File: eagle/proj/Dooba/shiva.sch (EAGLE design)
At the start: 55 parts, among them J1 DM3D-SFDM, J2 USB-BAMPHENOL-MICRO, U1 STM32F030X-LQFP48LQFP48, U2 TPS61200S-PVSON-N10, U3 MAX1811SO8, U4 FT232RQFN32, U5 SN74LVC1G125SOT23-5, U6 SN74LVC1G125SOT23-5, U7 LP3985SOT23-5, U8 LP3985SOT23-5, X1 8MHz

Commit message: Added some parts to Eagle Library Further designed Shiva MP3 Player schematic
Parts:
- added C30, C31: 27pF, dooba:CAP0805
- added C32, C33, C34, C35, C36: 100nF, dooba:CAP0805
- added C37: 470pF, dooba:CAP0805
- added C38: 4.7nF, dooba:CAP0805
- added R11: 1M, dooba:RES0805
- added R12, R13: 4.7R, dooba:RES0805
- added R14: 10k, dooba:RES0805
- added R15: 1k, dooba:RES0805
- added U10: CS4334, dooba:CS4334
- added U11: LM4811PDSO-10, dooba:LM4811PDSO-10
- added U9: STA013LQFP44, dooba:STA013LQFP44
- added X2: 14.7456MHz, dooba:XTAL_GNDSMD_3225
- X1: value 8MHz -> 16MHz; device dooba:XTALSMD-5X32 -> dooba:XTAL_GNDSMD_3225
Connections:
- net N$10 renamed MICROSD_SCK
- net N$11 renamed MICROSD_MISO
- net N$12 renamed MICROSD_DET
- net N$29 renamed STM32F0_TX
- net N$30 renamed STM32F0_RX
- net N$8 renamed !MICROSD_CS
- net N$9 renamed MICROSD_MOSI
- net RX renamed FT232R_RX
- net TX renamed FT232R_TX
- net VIN renamed 5.5V
- removed net CTS: U4.!CTS
- new net 3.3V-CORE: C1.1, C11.1, C12.1, C13.1, C2.1, C26.1, C3.1, C32.2, C33.2, C34.2, C35.2, C4.1, C5.1, C6.2, C7.2, C8.1, R13.1, R14.2, U1.VCC@1, U1.VCC@24, U1.VCC@48, U1.VCCA, U5.!OE, U5.VCC, U7.VOUT, U9.!SRC_INT, U9.!TESTEN, U9.BIT_EN, U9.VDD_1, U9.VDD_2, U9.VDD_3, U9.VDD_4
- new net 3.3V-EXT: C14.2, C15.2, C16.2, C29.1, J1.VCC, R1.1, U8.VOUT
- new net N$11: C37.2, R15.1, U9.FILT
- new net N$2: C31.2, R11.1, U9.XTI, X2.1
- new net N$6: C36.1, R13.2, U9.PVDD
- new net N$8: R14.1, U9.!RESET
- new net N$9: C38.2, R15.2
- net GND: now also C30.1, C31.1, C32.1, C33.1, C34.1, C35.1, C37.1, C38.1, J1.DET_B, J1.GND, R12.2, U9.SCANEN, U9.VSS_1, U9.VSS_2, U9.VSS_3, U9.VSS_4, U9.VSS_5, X1.GND0, X1.GND1, X2.GND0, X2.GND1; no longer R1.1
- net N$3: now also C30.2, R11.2, U9.XTO, X2.2; no longer C14.2, C15.2, C16.2, C29.1, J1.DET_B, J1.VCC, U8.VOUT
- net N$7: now also C36.2, R12.1, U9.PVSS; no longer C1.1, C11.1, C12.1, C13.1, C2.1, C26.1, C3.1, C4.1, C5.1, C6.2, C7.2, C8.1, U1.VCC@1, U1.VCC@24, U1.VCC@48, U1.VCCA, U5.!OE, U5.VCC, U7.VOUT
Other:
- note added: "Boost Circuit Pumps up Battery Voltage to 5.5V"
- note added: "Core Regulator Provides 3.3V to Core Logic blocks: - STM32F030 - STA013"
- note added: "Extra Regulator Provides 3.3V to Extra blocks: - OLED Display - MicroSD Card"
- note added: "MicroSD Adapter Exposes SPI Interface to STM32F0"
- note added: "USB-Serial Level Switcher Bridges FT232R UART (5V) with STM32F0 UART (3.3V)"
- note removed: "Boost Circuit Pumps up Battery Voltage to 5.5V Serves VIN"
- moved on the sheet: BATT(VCC-GND), C10, C14, C15, C16, C21, C25, C26, C27, C28, C29, C9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

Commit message: Added OLED Display to Shiva MP3 Player Started adding button interface
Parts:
- added C39, C40, C41, C47, C48, C49, C50, C51, C52: CAP_POLARIZEDSMD_RADIAL_43, dooba:CAP_POLARIZEDSMD_RADIAL_43
- added C42, C43, C44: CAP0805, dooba:CAP0805
- added C45, C46: 1uF, dooba:CAP0805
- added J3: SJ1-3523N, dooba:SJ1-3523N
- added J4: ADAFRUIT_OLED_13, dooba:ADAFRUIT_OLED_13
- added R16, R17, R18, R19, R22: RES0805, dooba:RES0805
- added R20, R21, R23, R24, R25, R26, R27, R28, R29: 10k, dooba:RES0805
- added SW1: LEFT, dooba:TACTSWCK_PTS_830
- added SW2: UP, dooba:TACTSWCK_PTS_830
- added SW3: CENTER, dooba:TACTSWCK_PTS_830
- added SW4: DOWN, dooba:TACTSWCK_PTS_830
- added SW5: RIGHT, dooba:TACTSWCK_PTS_830
- added SW6: VOL_UP, dooba:TACTSWCK_PTS_830
- added SW7: VOL_DN, dooba:TACTSWCK_PTS_830
- added U12: 5.0V, dooba:LP3985SOT23-5
- U7, U8: value LP3985SOT23-5 -> 3.3V
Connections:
- net 3.3V-EXT renamed 3.3V-MICROSD
- new net !STA013_RST: R14.1, U1.PA3, U9.!RESET
- new net 5.0V-AUDIO: C39.2, C42.1, C46.1, C47.2, R22.2, U10.VA, U11.VCC, U12.VOUT
- new net AMP_SHUTDOWN: R22.1, U1.PA2, U11.SHUTDOWN
- new net AMP_VOL_CLK: U1.PA1, U11.CLOCK
- new net AMP_VOL_UPDN: U1.PA0, U11.UP/DN
- new net AOUT_L: C43.1, C51.1, R17.2
- new net AOUT_R: C44.2, C52.1, R16.2
- new net I2C_SCL: J4.CLK, R20.2, U1.PB6, U9.SCL
- new net I2C_SDA: J4.DATA, R21.2, U1.PB7, U9.SDA
- new net N$10: C40.2, R18.1, U10.AOUTL
- new net N$12: C41.2, R19.2, U10.AOUTR
- new net N$28: C41.1, R16.1
- new net N$29: C40.1, R17.1
- new net N$30: C48.2, U11.VOUT1
- new net N$31: C49.2, U11.VOUT2
- new net N$32: C50.2, U11.BYPASS
- new net N$34: C49.1, J3.RING
- new net N$39: C51.2, U11.VIN1
- new net N$40: C52.2, U11.VIN2
- new net OLED_RST: J4.RST, U1.PA4
- new net STA013_DREQ: U1.PA6, U9.OUT_CLK/DATA_REC
- new net STA013_LRCKT: U10.LRCK, U9.LRCKT
- new net STA013_OCLK: U10.MCLK, U9.OCLK
- new net STA013_SCKR: U1.PA5, U9.SCKR
- new net STA013_SCKT: U10.DEM/SCLK, U9.SCKT
- new net STA013_SDI: U1.PA7, U9.SDI
- new net STA013_SDO: U10.SDATA, U9.SDO
- net 5.5V: now also C45.1, J4.VIN, U12.EN, U12.VIN
- net GND: now also C39.1, C42.2, C43.2, C44.1, C45.2, C46.2, C47.1, C50.1, J3.SLEEVE, J4.GND, R18.2, R19.1, R20.1, R21.1, U10.AGND, U11.GND, U12.GND
- net N$8: now also C48.1, J3.TIP; no longer R14.1, U9.!RESET
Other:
- note added: "128x64 Monochrome OLED Provides UI"
- note added: "Audio Regulator Provides 5.0V to Audio blocks: - D/A Converter - Headphone Amp"
- note added: "CS4334 DAC Converts Digital Audio from STA013 Feeds Analog Audio to Headphone Amplifier"
- note added: "LM4811 Headphone Amplifier Provides Volume Control"
- note added: "MicroSD Regulator Provides 3.3V to the MicroSD Card"
- note added: "STA013 MP3 Decoder Provides Digital Audio Output to DAC"
- note removed: "Extra Regulator Provides 3.3V to Extra blocks: - OLED Display - MicroSD Card"
- moved on the sheet: BATT(VCC-GND), C1, C10, C11, C12, C13, C14, C15, C16, C17, C18, C19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

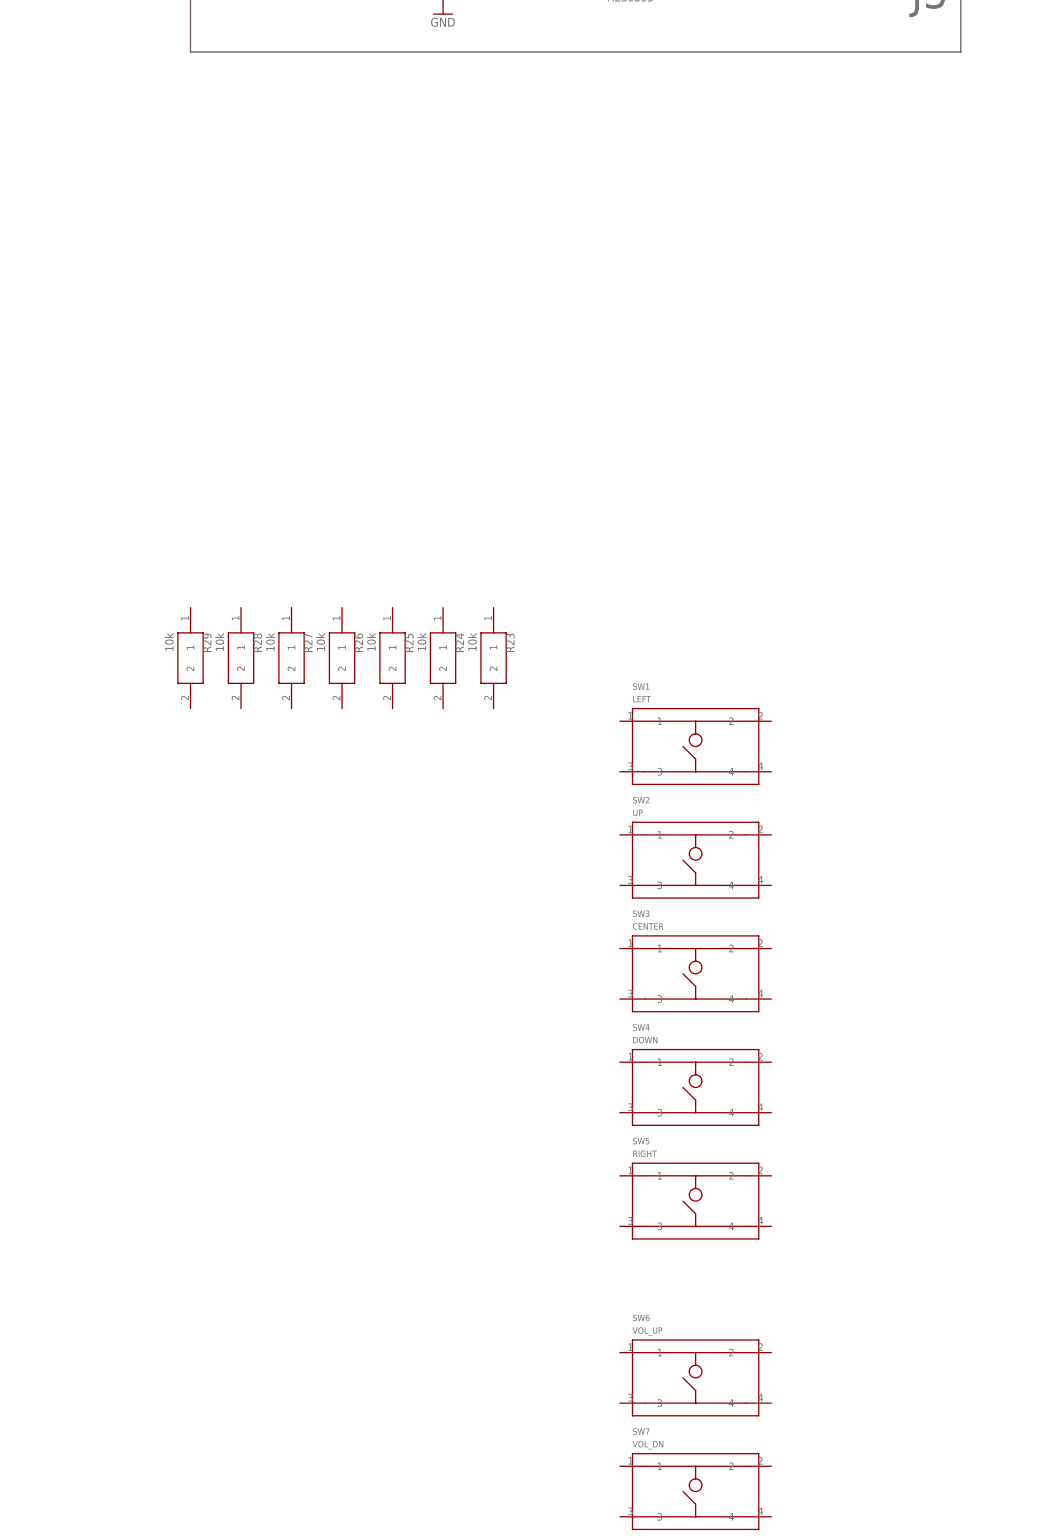
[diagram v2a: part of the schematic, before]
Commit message: Further designed Shiva MP3 Player Schematic Added MCP23008 I2C I/O Expander to Eagle Library
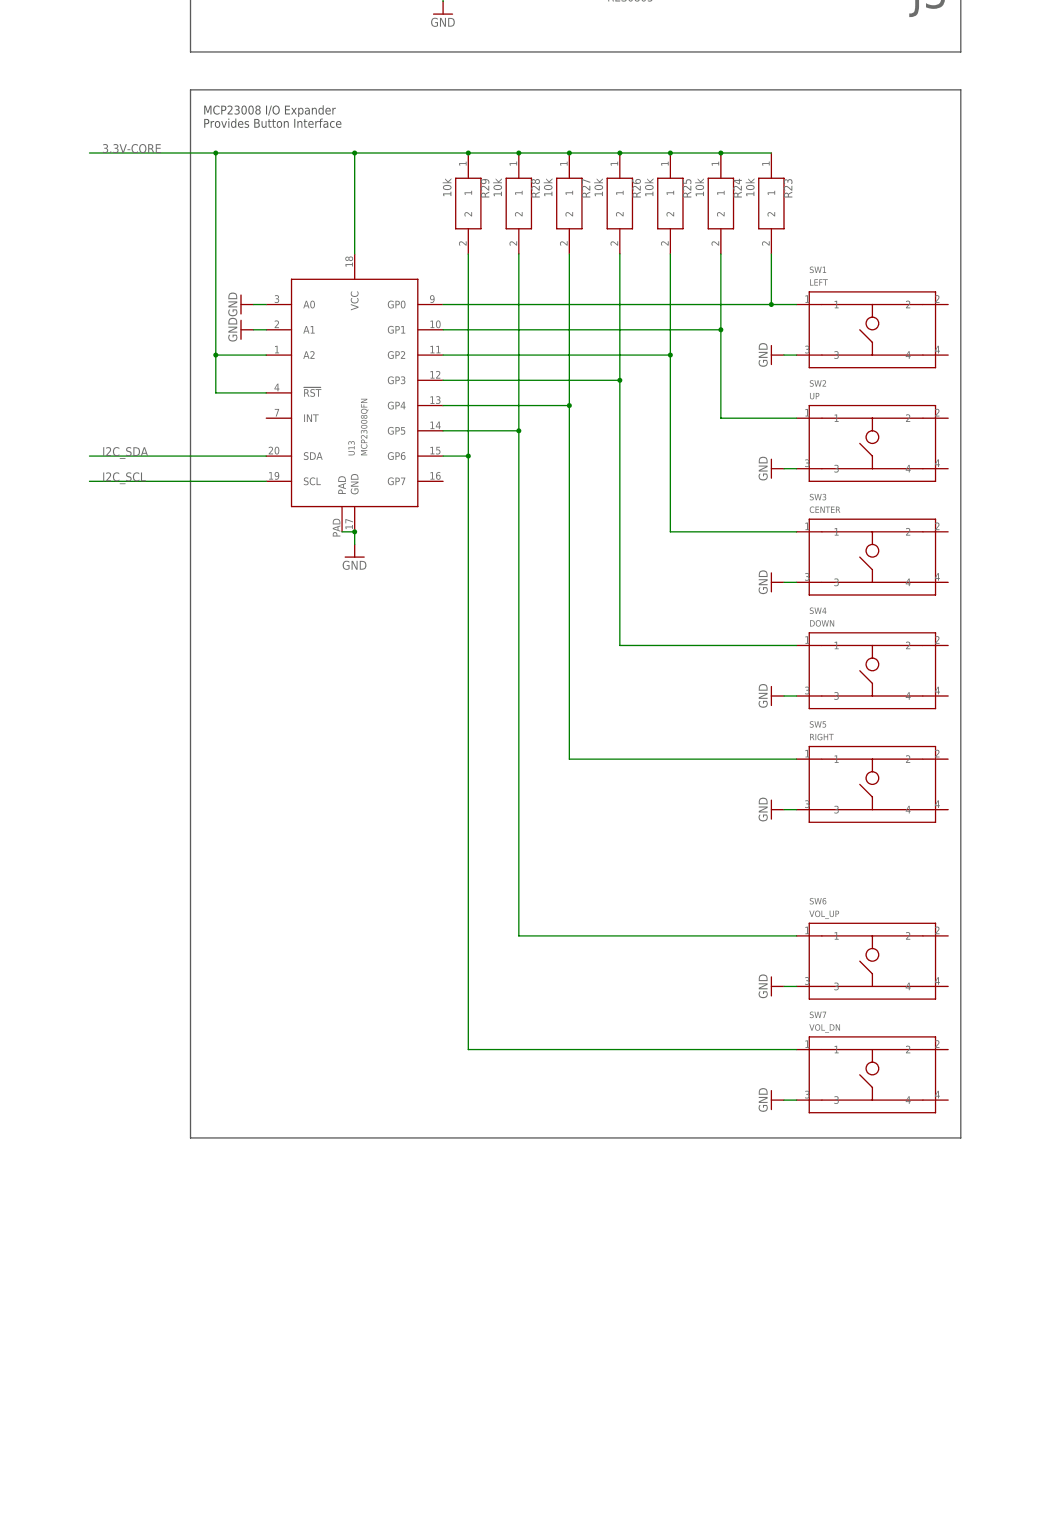
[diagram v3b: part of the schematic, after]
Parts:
- added U13: MCP23008QFN, dooba:MCP23008QFN
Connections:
- new net N$33: R23.2, SW1.1, U13.GP0
- new net N$35: R24.2, SW2.1, U13.GP1
- new net N$36: R25.2, SW3.1, U13.GP2
- new net N$37: R26.2, SW4.1, U13.GP3
- new net N$38: R27.2, SW5.1, U13.GP4
- new net N$41: R28.2, SW6.1, U13.GP5
- new net N$42: R29.2, SW7.1, U13.GP6
- net 3.3V-CORE: now also R23.1, R24.1, R25.1, R26.1, R27.1, R28.1, R29.1, U13.!RST, U13.A2, U13.VCC
- net GND: now also SW1.3, SW2.3, SW3.3, SW4.3, SW5.3, SW6.3, SW7.3, U13.A0, U13.A1, U13.GND, U13.PAD
- net I2C_SCL: now also U13.SCL
- net I2C_SDA: now also U13.SDA
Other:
- note added: "MCP23008 I/O Expander Provides Button Interface"
- moved on the sheet: R23, R24, R25, R26, R27, R28, R29, SW1, SW2, SW3, SW4, SW5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
